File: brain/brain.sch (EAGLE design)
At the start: 4 parts

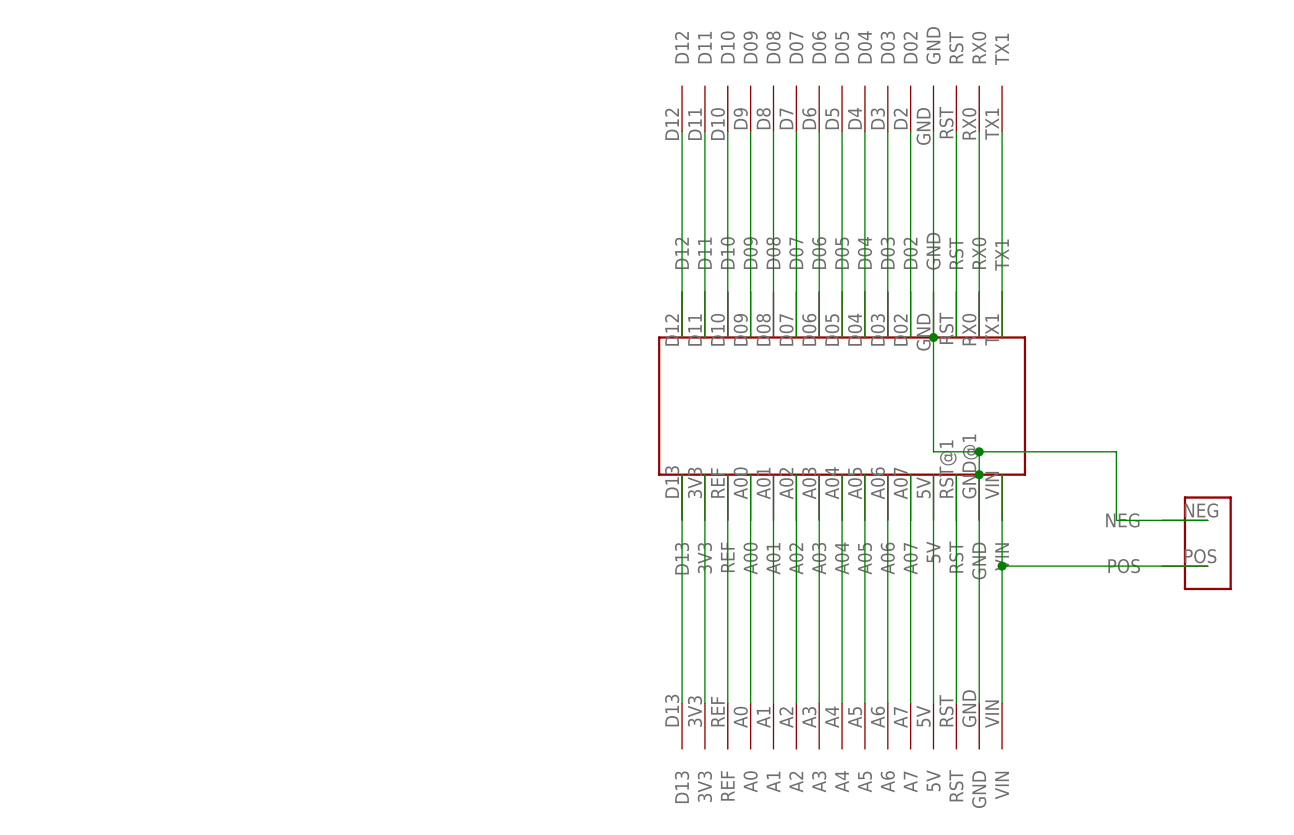
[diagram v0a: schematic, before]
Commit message: Added decoupling capacitors to brain board. Also adjusted the origin to be in the bottom left corner of the PCB.
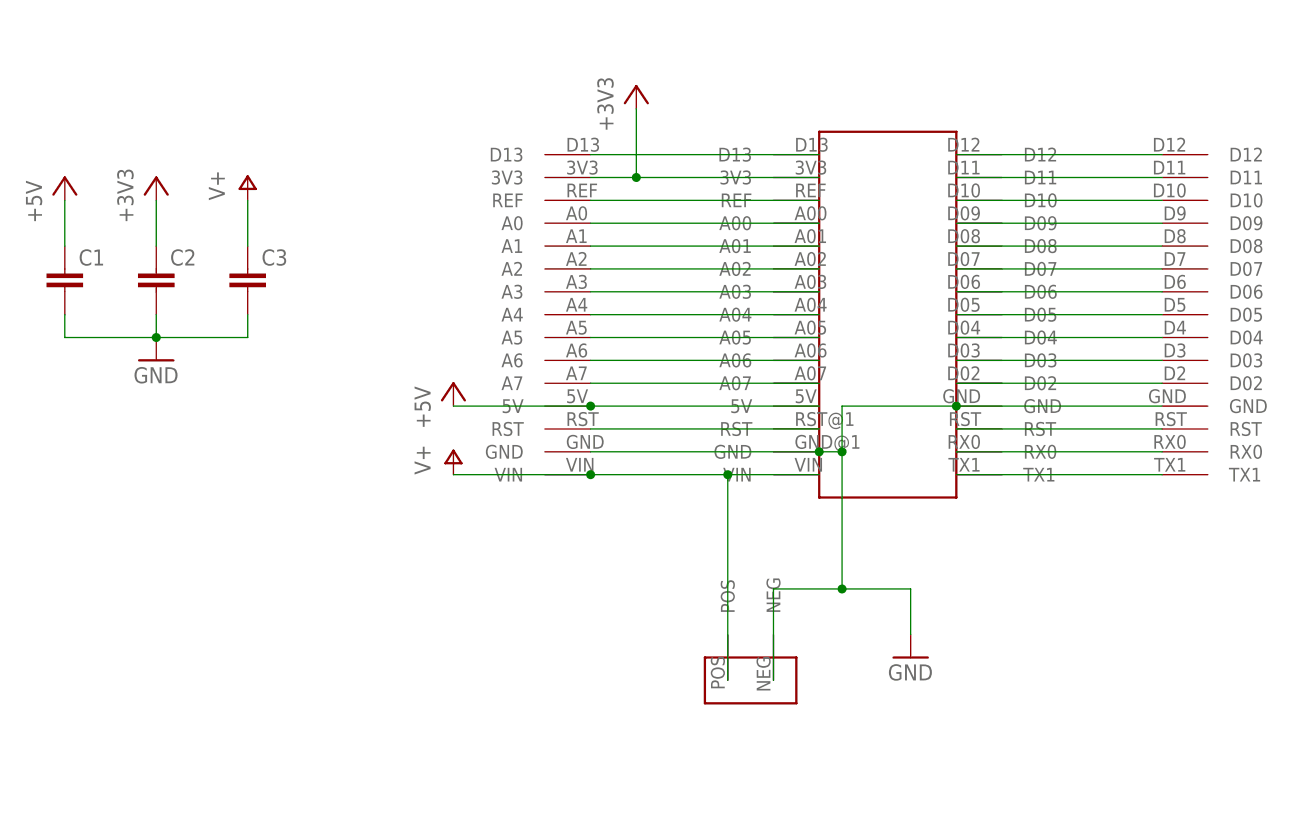
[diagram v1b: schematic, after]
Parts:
- added C1, C2, C3: (no value), rcl:C-EU050-025X075
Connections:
- removed net 3V3: U$1.3V3, U$5.3V3
- removed net 5V: U$1.5V, U$5.5V
- removed net VIN: U$1.VIN, U$3.POS, U$5.VIN
- new net +3V3: C2.1, U$1.3V3, U$5.3V3
- new net +5V: C1.1, U$1.5V, U$5.5V
- new net V+: C3.1, U$1.VIN, U$3.POS, U$5.VIN
- net GND: now also C1.2, C2.2, C3.2
